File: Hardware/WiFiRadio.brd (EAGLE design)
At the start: 65.7 x 25.4 mm, 55 parts, among them IC1 VS1053B, IC2 23LCV1024-I/SN, IC3 MCP1703AT-1802E/CB, IC4 MCP1703AT-3302E/CB, J1 ADC, J2 RAM, K1 STX-3100-5N, K2 SERIAL, K3 PANEL, K4 POWER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

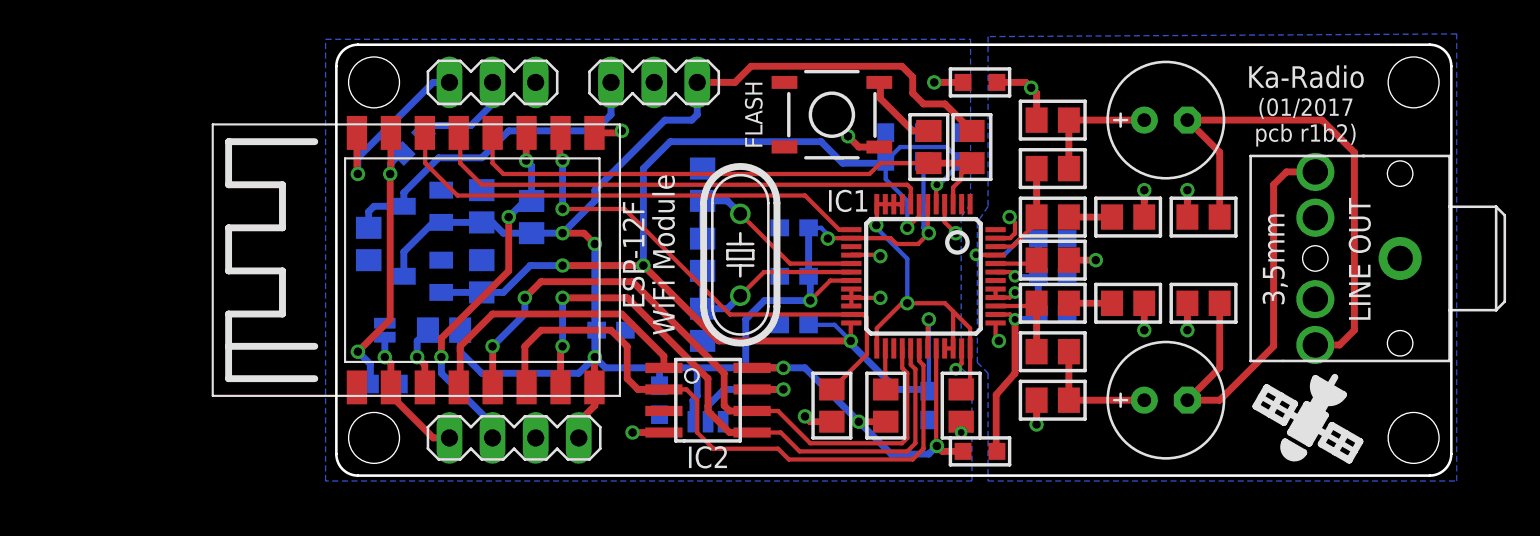
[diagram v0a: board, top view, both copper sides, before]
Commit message: new (smaller) pcb for personal needs, removed 5v and 3v3 regulators, added other small improvements
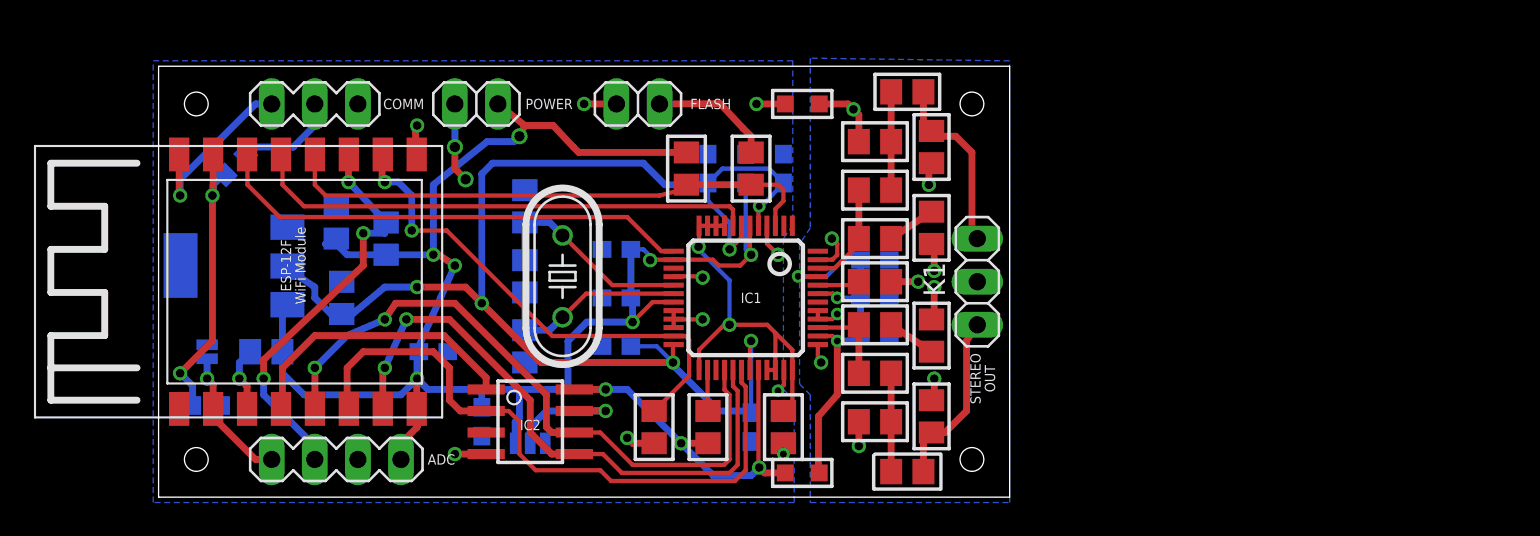
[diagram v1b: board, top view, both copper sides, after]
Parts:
- removed C12: 10μ, rcl:C0805
- removed IC3: MCP1703AT-1802E/CB, linear:SOT23
- C10, C9: device rcl:E2,5-7 -> rcl:C0805
- IC4: value MCP1703AT-3302E/CB -> 1117-1.8; device linear:SOT23 -> burr-brown:SOT223
- K1: value STX-3100-5N -> STEREO; device adafruit:STX3100 -> pinhead:1X03
- K4: device con-lstb:MA03-1 -> pinhead:1X02
- S1: device SparkFun-Electromechanical:TACTILE-SWITCH-SMD -> pinhead:1X02
- moved K1 27.7 mm to (48.3, 12.7), turned to 90 degrees
- moved R9 17.4 mm to (45.6, 4.76), turned to 270 degrees
- moved R3 16.9 mm to (31.1, 19.4)
- moved R8 16.6 mm to (45.6, 20.6), turned to 270 degrees
- moved C9 15.8 mm to (44.1, 1.51)
- moved C10 15.3 mm to (44.1, 23.9)
- moved C39 11.7 mm to (45.6, 9.53), turned to 90 degrees
- moved IC4 11.6 mm to (4.45, 13.7)
- moved C46 11.6 mm to (45.6, 15.9), turned to 270 degrees
- moved S1 11.4 mm to (28.3, 23.2), turned to 0 degrees
- moved C31 10.6 mm to (34.9, 4.13)
- moved FB1 10.6 mm to (37.9, 1.43)
- moved FB2 10.6 mm to (37.9, 23.2)
- moved R10 10.6 mm to (34.9, 19.4)
- moved C14 10.6 mm to (27.0, 14.6)
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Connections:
- removed net 5V: C12.1, IC4.3, K4.1
- net +3V3: now also IC4.3, K4.1; no longer IC3.3, IC4.2, K4.3
- net 1.8V: now also IC4.2; no longer IC3.2
- net AGND: now also K1.2; no longer K1.1
- net GND: no longer C12.2, IC3.1
- net N$14: now also C9.2, K1.1; no longer C9.-, K1.5
- net N$15: now also C10.2, K1.3; no longer C10.-, K1.2
- net N$18: now also S1.2; no longer S1.3
- net N$7: now also C9.1; no longer C9.+
- net N$8: now also C10.1; no longer C10.+
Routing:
- net 5V: track 20.0 -> 0.00 mm
- net N$15: track 30.3 -> 11.2 mm
- net N$14: track 25.2 -> 10.4 mm
- net +3V3: track 134.4 -> 124.2 mm, vias 9 -> 10
- net GND: track 17.5 -> 22.1 mm, vias 10 -> 12
- net N$18: track 4.63 -> 7.18 mm
- net LED: track 21.8 -> 23.9 mm
- net N$8: track 7.30 -> 5.79 mm
- net N$7: track 7.30 -> 5.79 mm
- net 1.8V: track 78.3 -> 79.6 mm
- net MOSI: track 36.9 -> 35.9 mm
- net SCK: track 39.6 -> 39.0 mm
- net AGND: track 18.8 -> 19.4 mm
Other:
- board size 65.7 x 25.4 mm -> 50.2 x 25.4 mm
- board text added: "COMM"
- board text added: "KA-RADIO UKRAINE 2017"
- board text added: "POWER"
- board text added: "STEREO OUT"
- board text removed: "(01/2017 pcb r1b2)"
- board text removed: "(C) 2017 DIMITRIS SALTAS"
- board text removed: "3V3 OR 5V NOT BOTH"
- board text removed: "5V"
- board text removed: "IC3"
- board text removed: "IC4"
- board text removed: "Ka-Radio"
- board text removed: "Ka-Radio Project github.com/karawin/Ka-Radio"
- board text removed: "LEFT"
- board text removed: "LINE OUT"
- board text removed: "RIGHT"
- board text removed: "SALTECH INSTRUMENTS IANOYAPIOΣ 2017"
